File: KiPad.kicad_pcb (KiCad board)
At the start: 2 copper layers, 82 x 142.5 mm, 67 parts, among them J1 USB_C_Receptacle_USB2.0, SW1 SW_SPST_LED, SW10 SW_SPST, SW11 SW_SPST, SW12 SW_SPST, SW13 SW_SPST, SW14 SW_SPST, SW15 SW_SPST, SW16 SW_SPST, SW17 SW_SPST, SW18 SW_SPST, SW19 SW_SPST, SW2 SW_SPST_LED, SW20 SW_SPST, SW21 SW_SPST, SW3 SW_SPST_LED, SW4 SW_SPST_LED, SW5 SW_SPST, SW6 SW_SPST, SW7 SW_SPST, SW8 SW_SPST, SW9 SW_SPST, U1 ATmega32U4RC-A, Y1 16MHz

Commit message: v2
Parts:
- removed C1: 1u, Capacitor_SMD:C_0805_2012Metric
- removed C3, C4: 22p, Capacitor_SMD:C_0805_2012Metric
- removed the D21 at (155.0, 117.2)
- removed the D21 at (104.4, 116.9)
- removed F1: 500mA, Fuse:Fuse_1206_3216Metric
- removed R1, R2: 22, Resistor_SMD:R_0805_2012Metric
- removed R10, R11: 10k, Resistor_SMD:R_0805_2012Metric
- removed R3, R4: 5.1k, Resistor_SMD:R_0805_2012Metric
- removed SW_HWB1, SW_RST1: SW_Push, Button_Switch_SMD:SW_SPST_TL3342
- removed U1: ATmega32U4RC-A, Package_QFP:TQFP-44_10x10mm_P0.8mm
- removed Y1: 16MHz, Crystal:Crystal_SMD_3225-4Pin_3.2x2.5mm
- added D21: ~, Diode_SMD:D_MiniMELF, B.Cu at (100.3, 43.1)
- added J2: Conn_02x08_Counter_Clockwise, Connector_PinSocket_2.54mm:PinSocket_2x08_P2.54mm_Vertical, F.Cu at (149.5, 78.8)
- added kibuzzard-66936F3A: G***, kibuzzard-66936F3A, F.Cu at (36.0, 24.0)
- added kibuzzard-66936F5C: G***, kibuzzard-66936F5C, F.Cu at (45.5, 25.5)
- added kibuzzard-66936F83: G***, kibuzzard-66936F83, F.Cu at (93.8, 149.2)
- added kibuzzard-669374CF: G***, kibuzzard-669374CF, F.Cu at (143.5, 57.5)
- added kibuzzard-669374E3: G***, kibuzzard-669374E3, F.Cu at (144.8, 50.0)
- added kibuzzard-66937522: G***, kibuzzard-66937522, F.Cu at (145.8, 54.2)
- added kibuzzard-6693755C: G***, kibuzzard-6693755C, F.Cu at (154.0, 87.2)
- A1: footprint Custom:KB2040_SMD -> Custom:KB2040_THT
- C2, C5, R6, R7, R8, R9: moved to B.Cu
- J1: value USB_C_Receptacle_USB2.0 -> Conn_02x08_Counter_Clockwise; footprint Connector_USB:USB_C_Receptacle_GCT_USB4105-xx-A_16P_TopMnt_Horizontal -> Connector_PinSocket_2.54mm:PinSocket_2x08_P2.54mm_Vertical
- SW1, SW2, SW3, SW4: footprint Custom:MX-Solderable-1U-0805-LED -> Custom:MX-Hotswap-1U-0805-LED
- SW10, SW11, SW13, SW14, SW15, SW16, SW17, SW18, SW21, SW5, SW6, SW7, SW8, SW9: footprint MX_Solderable:MX-Solderable-1U -> MX_Hotswap:MX-Hotswap-1U
- SW12, SW19: footprint MX_Solderable:MX-Solderable-2U-Vertical -> MX_Hotswap:MX-Hotswap-2U-Vertical-ReversedStabilizers
- SW20: footprint MX_Solderable:MX-Solderable-2U -> MX_Hotswap:MX-Hotswap-2U
- moved R9 79.6 mm to (95.2, 43.5)
- moved R6 79.6 mm to (38.2, 43.5)
- moved R7 79.6 mm to (57.2, 43.5)
- moved R8 79.6 mm to (76.2, 43.5)
- moved D8 73.9 mm to (100.3, 95.5)
- moved SW12 73.9 mm to (95.2, 90.5)
- moved D1 73.9 mm to (43.2, 66.9)
- moved D12 73.9 mm to (43.2, 124.1)
- moved D13 73.9 mm to (62.2, 124.1)
- moved D14 73.9 mm to (81.3, 124.1)
- moved D15 73.9 mm to (100.3, 133.6)
- moved D16 73.9 mm to (52.7, 143.1)
- moved D17 73.9 mm to (81.3, 143.1)
- moved D18 73.9 mm to (43.2, 43.1)
- moved D19 73.9 mm to (62.2, 43.1)
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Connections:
- A1 pad 10: /R2 -> /MCU_C1
- A1 pad 11: /R3 -> /MCU_C2
- A1 pad 12: /R4 -> /MCU_C3
- A1 pad 13: /R5 -> /MCU_R0
- A1 pad 14: unconnected-(A1-D10-Pad14) -> /MCU_R1
- A1 pad 18: /LED_A -> /MCU_LED_A
- A1 pad 19: /LED_B -> /MCU_LED_B
- A1 pad 2: /C0 -> unconnected-(A1-D0-Pad2)
- A1 pad 20: /LED_C -> /MCU_LED_C
- A1 pad 21: /LED_D -> /MCU_LED_D
- A1 pad 22: +5V -> /MCU_VCC
- A1 pad 24: GND -> /MCU_GND
- A1 pad 3: /C1 -> /MCU_R2
- A1 pad 4: GND -> /MCU_GND
- A1 pad 5: GND -> /MCU_GND
- A1 pad 6: /C2 -> /MCU_R3
- A1 pad 7: /C3 -> /MCU_R4
- A1 pad 8: /R0 -> /MCU_R5
- A1 pad 9: /R1 -> /MCU_C0
- C2 pad 1: +5V -> +3V3
- C5 pad 1: +5V -> +3V3
- C6 pad 1: +5V -> +3V3
- C7 pad 1: +5V -> +3V3
- SW1 pad 4: +5V -> +3V3
- SW2 pad 4: +5V -> +3V3
- SW3 pad 4: +5V -> +3V3
- SW4 pad 4: +5V -> +3V3
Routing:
- net +5V: track 205.8 -> 0.00 mm, vias 7 -> 0
- net +3V3: track 0.00 -> 85.4 mm, vias 0 -> 4
- net /C0: track 149.4 -> 216.6 mm, vias 1 -> 6
- net /MCU_R2: track 0.00 -> 65.7 mm
- net /R2: track 164.3 -> 101.1 mm
- net /R1: track 131.2 -> 68.3 mm
- net /C1: track 109.7 -> 167.4 mm, vias 1 -> 5
- net /MCU_R3: track 0.00 -> 53.6 mm
- net /R4: track 202.3 -> 148.8 mm
- net /R3: track 165.4 -> 112.1 mm
- net /R5: track 194.0 -> 144.5 mm
- net GND: track 20.8 -> 68.7 mm, vias 5 -> 0
- net /MCU_R4: track 0.00 -> 46.5 mm
- net /MCU_C0: track 0.00 -> 39.8 mm
- net /MCU_R5: track 0.00 -> 39.2 mm
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- added copper zone on B.Cu, net /MCU_GND
- added copper zone on F.Cu, net /MCU_GND
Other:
- board size 82 x 142.5 mm -> 149.8 x 131.8 mm
- board text added: "JLCJLCJLCJLC"

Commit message: v3
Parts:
- removed A1: Adafruit Key Boar KB2040, Custom:KB2040_THT
- removed J2: Conn_02x08_Counter_Clockwise, Connector_PinSocket_2.54mm:PinSocket_2x08_P2.54mm_Vertical
- removed R6, R7, R8, R9: 470, Resistor_SMD:R_0805_2012Metric
- removed kibuzzard-66936F3A: G***, kibuzzard-66936F3A
- removed kibuzzard-66936F5C: G***, kibuzzard-66936F5C
- removed kibuzzard-66936F83: G***, kibuzzard-66936F83
- removed kibuzzard-669374CF: G***, kibuzzard-669374CF
- removed kibuzzard-669374E3: G***, kibuzzard-669374E3
- removed kibuzzard-66937522: G***, kibuzzard-66937522
- removed kibuzzard-6693755C: G***, kibuzzard-6693755C
- added C1: 22p, Capacitor_SMD:C_0402_1005Metric, B.Cu at (102.4, 120.5)
- added C3: 22p, Capacitor_SMD:C_0402_1005Metric, B.Cu at (102.2, 126.4)
- added LED1: SK6812MINI, Custom:LED_SK6812MINI-E_PLCC4_3.2x2.8mm_P1.75mm, B.Cu at (38.1, 32.6)
- added LED10: SK6812MINI, Custom:LED_SK6812MINI-E_PLCC4_3.2x2.8mm_P1.75mm, B.Cu at (57.1, 75.5)
- added LED11: SK6812MINI, Custom:LED_SK6812MINI-E_PLCC4_3.2x2.8mm_P1.75mm, B.Cu at (76.2, 75.5)
- added LED12: SK6812MINI, Custom:LED_SK6812MINI-E_PLCC4_3.2x2.8mm_P1.75mm, B.Cu at (95.2, 85.0)
- added LED13: SK6812MINI, Custom:LED_SK6812MINI-E_PLCC4_3.2x2.8mm_P1.75mm, B.Cu at (38.1, 94.5)
- added LED14: SK6812MINI, Custom:LED_SK6812MINI-E_PLCC4_3.2x2.8mm_P1.75mm, B.Cu at (57.1, 94.5)
- added LED15: SK6812MINI, Custom:LED_SK6812MINI-E_PLCC4_3.2x2.8mm_P1.75mm, B.Cu at (76.2, 94.5)
- added LED16: SK6812MINI, Custom:LED_SK6812MINI-E_PLCC4_3.2x2.8mm_P1.75mm, B.Cu at (38.1, 113.6)
- added LED17: SK6812MINI, Custom:LED_SK6812MINI-E_PLCC4_3.2x2.8mm_P1.75mm, B.Cu at (57.1, 113.6)
- added LED18: SK6812MINI, Custom:LED_SK6812MINI-E_PLCC4_3.2x2.8mm_P1.75mm, B.Cu at (76.2, 113.6)
- added LED19: SK6812MINI, Custom:LED_SK6812MINI-E_PLCC4_3.2x2.8mm_P1.75mm, B.Cu at (95.2, 123.1)
- added LED2: SK6812MINI, Custom:LED_SK6812MINI-E_PLCC4_3.2x2.8mm_P1.75mm, B.Cu at (57.1, 32.6)
- added LED20: SK6812MINI, Custom:LED_SK6812MINI-E_PLCC4_3.2x2.8mm_P1.75mm, B.Cu at (47.6, 132.6)
- added LED21: SK6812MINI, Custom:LED_SK6812MINI-E_PLCC4_3.2x2.8mm_P1.75mm, B.Cu at (76.2, 132.6)
- added LED3: SK6812MINI, Custom:LED_SK6812MINI-E_PLCC4_3.2x2.8mm_P1.75mm, B.Cu at (76.2, 32.6)
- added LED4: SK6812MINI, Custom:LED_SK6812MINI-E_PLCC4_3.2x2.8mm_P1.75mm, B.Cu at (95.2, 32.6)
- added LED5: SK6812MINI, Custom:LED_SK6812MINI-E_PLCC4_3.2x2.8mm_P1.75mm, B.Cu at (38.1, 56.4)
- added LED6: SK6812MINI, Custom:LED_SK6812MINI-E_PLCC4_3.2x2.8mm_P1.75mm, B.Cu at (57.1, 56.4)
- added LED7: SK6812MINI, Custom:LED_SK6812MINI-E_PLCC4_3.2x2.8mm_P1.75mm, B.Cu at (76.2, 56.4)
- added LED8: SK6812MINI, Custom:LED_SK6812MINI-E_PLCC4_3.2x2.8mm_P1.75mm, B.Cu at (95.2, 56.4)
- added LED9: SK6812MINI, Custom:LED_SK6812MINI-E_PLCC4_3.2x2.8mm_P1.75mm, B.Cu at (38.1, 75.5)
- added R1: 10k, Resistor_SMD:R_0402_1005Metric, B.Cu at (92.6, 105.3)
- added R2: 5.1k, Resistor_SMD:R_0402_1005Metric, F.Cu at (67.6, 28.6)
- added R3: 5.1k, Resistor_SMD:R_0402_1005Metric, F.Cu at (65.7, 28.6)
- added R4: 22, Resistor_SMD:R_0402_1005Metric, B.Cu at (66.0, 35.0)
- added R5: 22, Resistor_SMD:R_0402_1005Metric, B.Cu at (67.4, 35.0)
- added SW22: RESET, Resistor_SMD:R_0603_1608Metric, B.Cu at (91.2, 104.7)
- added U2: ATmega32U2-M, Package_DFN_QFN:QFN-32-1EP_5x5mm_P0.5mm_EP3.1x3.1mm, B.Cu at (96.4, 108.8)
- added Y1: 16MHz, Crystal:Crystal_SMD_3225-4Pin_3.2x2.5mm, B.Cu at (102.3, 123.5)
- added kibuzzard-669F6A5B: G***, kibuzzard-669F6A5B, F.Cu at (93.4, 27.4)
- added kibuzzard-669F6A5B: G***, kibuzzard-669F6A5B, B.Cu at (41.0, 27.4)
- added kibuzzard-669F6A61: G***, kibuzzard-669F6A61, F.Cu at (101.0, 28.3)
- added kibuzzard-669F6A61: G***, kibuzzard-669F6A61, B.Cu at (33.3, 28.3)
- added kibuzzard-669F6A7B: G***, kibuzzard-669F6A7B, F.Cu at (36.9, 148.8)
- added kibuzzard-669F6A7B: G***, kibuzzard-669F6A7B, B.Cu at (96.5, 148.8)
- C6: value 0.1u -> 1u; footprint Capacitor_SMD:C_0805_2012Metric -> Capacitor_SMD:C_0603_1608Metric
- J1: value Conn_02x08_Counter_Clockwise -> USB_C_Receptacle_USB2.0_14P; footprint Connector_PinSocket_2.54mm:PinSocket_2x08_P2.54mm_Vertical -> Connector_USB:USB_C_Receptacle_GCT_USB4105-xx-A_16P_TopMnt_Horizontal
- SW1: value SW_SPST_LED -> SW_A; footprint Custom:MX-Hotswap-1U-0805-LED -> MX_Hotswap:MX-Hotswap-1U
- SW10: value SW_SPST -> SW_8
- SW11: value SW_SPST -> SW_9
- SW12: value SW_SPST -> SW_ADD
- SW13: value SW_SPST -> SW_4
- SW14: value SW_SPST -> SW_5
- SW15: value SW_SPST -> SW_6
- SW16: value SW_SPST -> SW_1
- SW17: value SW_SPST -> SW_2
- SW18: value SW_SPST -> SW_3
- SW19: value SW_SPST -> SW_ENTER
- SW2: value SW_SPST_LED -> SW_B; footprint Custom:MX-Hotswap-1U-0805-LED -> MX_Hotswap:MX-Hotswap-1U
- SW20: value SW_SPST -> SW_0
- SW21: value SW_SPST -> SW_DOT
- SW3: value SW_SPST_LED -> SW_C; footprint Custom:MX-Hotswap-1U-0805-LED -> MX_Hotswap:MX-Hotswap-1U
- SW4: value SW_SPST_LED -> SW_D; footprint Custom:MX-Hotswap-1U-0805-LED -> MX_Hotswap:MX-Hotswap-1U
- SW5: value SW_SPST -> SW_NL
- SW6: value SW_SPST -> SW_DIV
- SW7: value SW_SPST -> SW_MUL
- SW8: value SW_SPST -> SW_SUB
- SW9: value SW_SPST -> SW_7
- moved D20 105.3 mm to (55.8, 145.3)
- moved D21 103.4 mm to (84.4, 145.3)
- moved D19 101.4 mm to (103.4, 135.8)
- moved D18 92.8 mm to (84.4, 126.3)
- moved D12 59.0 mm to (96.6, 99.1), turned to 0 degrees
- moved C6 57.4 mm to (94.8, 103.4), turned to 90 degrees
- moved C7 57.3 mm to (102.4, 105.7), turned to 0 degrees
- moved J1 43.5 mm to (66.7, 28.6), turned to 0 degrees
- moved C2 33.9 mm to (70.3, 35.7), turned to 0 degrees
- moved D15 30.8 mm to (84.4, 107.2)
- moved D8 26.6 mm to (103.4, 69.1)
- moved D17 23.2 mm to (65.3, 126.3)
- moved D14 23.2 mm to (65.3, 107.2)
- moved D13 23.2 mm to (46.3, 107.2)
- moved D1 21.9 mm to (46.3, 45.3)
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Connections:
- C2 pad 1: +3V3 -> +5V
- C5 pad 1: +3V3 -> +5V
- C6 pad 1: +3V3 -> Net-(U2-UCAP)
- C7 pad 1: +3V3 -> +5V
- D1 pad 1: /R1 -> /R0
- D10 pad 1: /R3 -> /R2
- D11 pad 1: /R3 -> /R2
- D12 pad 1: /R4 -> /R2
- D13 pad 1: /R4 -> /R3
- D14 pad 1: /R4 -> /R3
- D15 pad 1: /R4 -> /R3
- D16 pad 1: /R5 -> /R4
- D17 pad 1: /R5 -> /R4
- D18 pad 1: /R0 -> /R4
- D19 pad 1: /R0 -> /R4
- D2 pad 1: /R1 -> /R0
- D20 pad 1: /R0 -> /R5
- D21 pad 1: /R0 -> /R5
- D3 pad 1: /R1 -> /R0
- D4 pad 1: /R1 -> /R0
- D5 pad 1: /R2 -> /R1
- D6 pad 1: /R2 -> /R1
- D7 pad 1: /R2 -> /R1
- D8 pad 1: /R2 -> /R1
- D9 pad 1: /R3 -> /R2
- SW1 pad 1: Net-(D18-A) -> Net-(D1-A)
- SW10 pad 1: Net-(D6-A) -> Net-(D10-A)
- SW11 pad 1: Net-(D7-A) -> Net-(D11-A)
- SW12 pad 1: Net-(D8-A) -> Net-(D12-A)
- SW13 pad 1: Net-(D9-A) -> Net-(D13-A)
- SW14 pad 1: Net-(D10-A) -> Net-(D14-A)
- SW15 pad 1: Net-(D11-A) -> Net-(D15-A)
- SW16 pad 1: Net-(D12-A) -> Net-(D16-A)
- SW17 pad 1: Net-(D13-A) -> Net-(D17-A)
- SW18 pad 1: Net-(D14-A) -> Net-(D18-A)
- SW19 pad 1: Net-(D15-A) -> Net-(D19-A)
- SW2 pad 1: Net-(D19-A) -> Net-(D2-A)
- SW20 pad 1: Net-(D16-A) -> Net-(D20-A)
- SW21 pad 1: Net-(D17-A) -> Net-(D21-A)
- SW3 pad 1: Net-(D20-A) -> Net-(D3-A)
- SW4 pad 1: Net-(D21-A) -> Net-(D4-A)
- SW5 pad 1: Net-(D1-A) -> Net-(D5-A)
- SW6 pad 1: Net-(D2-A) -> Net-(D6-A)
- SW7 pad 1: Net-(D3-A) -> Net-(D7-A)
- SW8 pad 1: Net-(D4-A) -> Net-(D8-A)
- SW9 pad 1: Net-(D5-A) -> Net-(D9-A)
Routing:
- net +5V: track 0.00 -> 513.8 mm, vias 0 -> 9
- net /LED_DATA: track 0.00 -> 159.7 mm, vias 0 -> 4
- net /USB_DP: track 0.00 -> 103.3 mm, vias 0 -> 4
- net /USB_DN: track 0.00 -> 102.5 mm, vias 0 -> 2
- net +3V3: track 85.4 -> 0.00 mm, vias 4 -> 0
- net /LED_A: track 79.5 -> 0.00 mm, vias 2 -> 0
- net Net-(LED4-DOUT): track 0.00 -> 76.2 mm
- net Net-(LED8-DOUT): track 0.00 -> 75.4 mm
- net /R0: track 63.8 -> 135.9 mm, vias 0 -> 2
- net Net-(LED12-DOUT): track 0.00 -> 66.7 mm
- net /MCU_R2: track 65.7 -> 0.00 mm
- net /R3: track 112.1 -> 48.1 mm
- net Net-(LED19-DOUT): track 0.00 -> 62.5 mm
- net /LED_B: track 59.4 -> 0.00 mm, vias 2 -> 0
- net Net-(LED15-DOUT): track 0.00 -> 55.5 mm
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- removed copper zone on B.Cu, net /MCU_GND
- removed copper zone on F.Cu, net /MCU_GND
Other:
- board size 149.8 x 131.8 mm -> 81.9 x 126.7 mm
- board text removed: "JLCJLCJLCJLC"

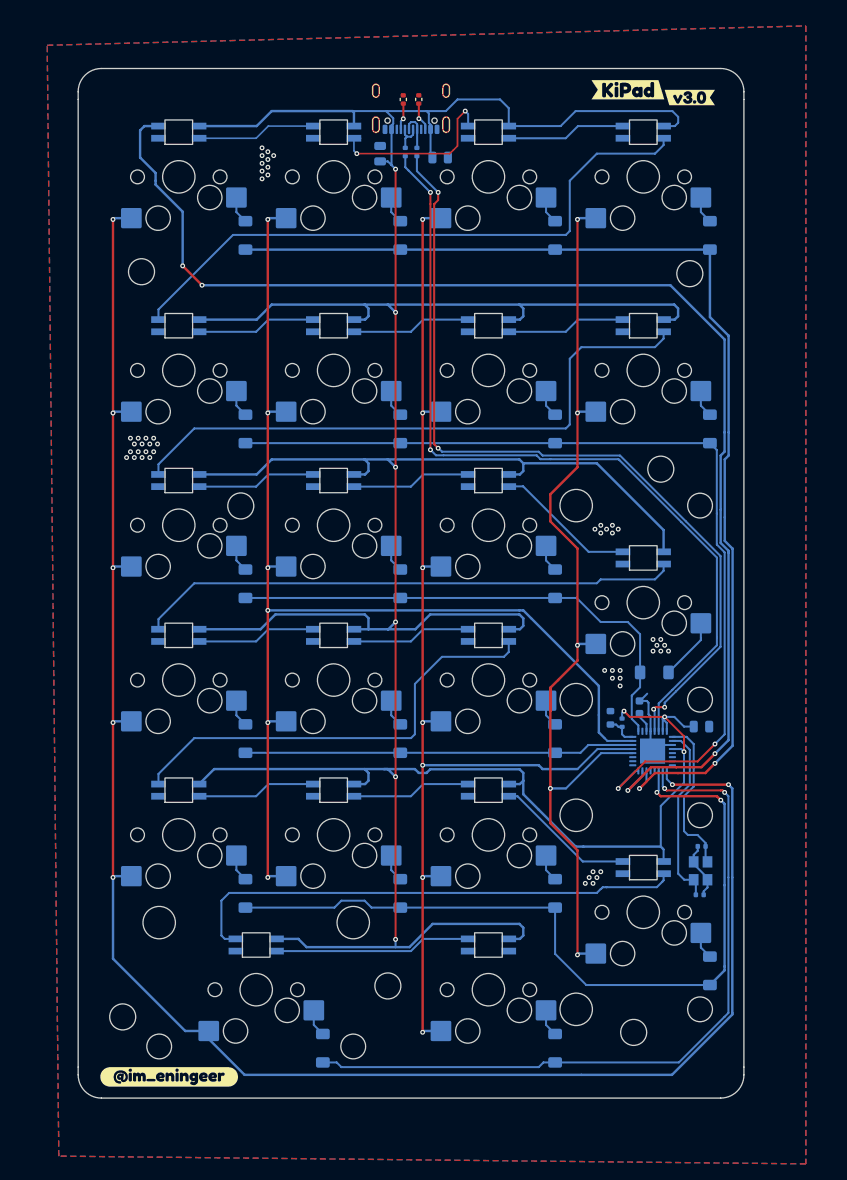
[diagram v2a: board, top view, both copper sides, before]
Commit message: v3.1
Flip around stabs so the shaft is on the outside.
Fix LED footprint and reroute.
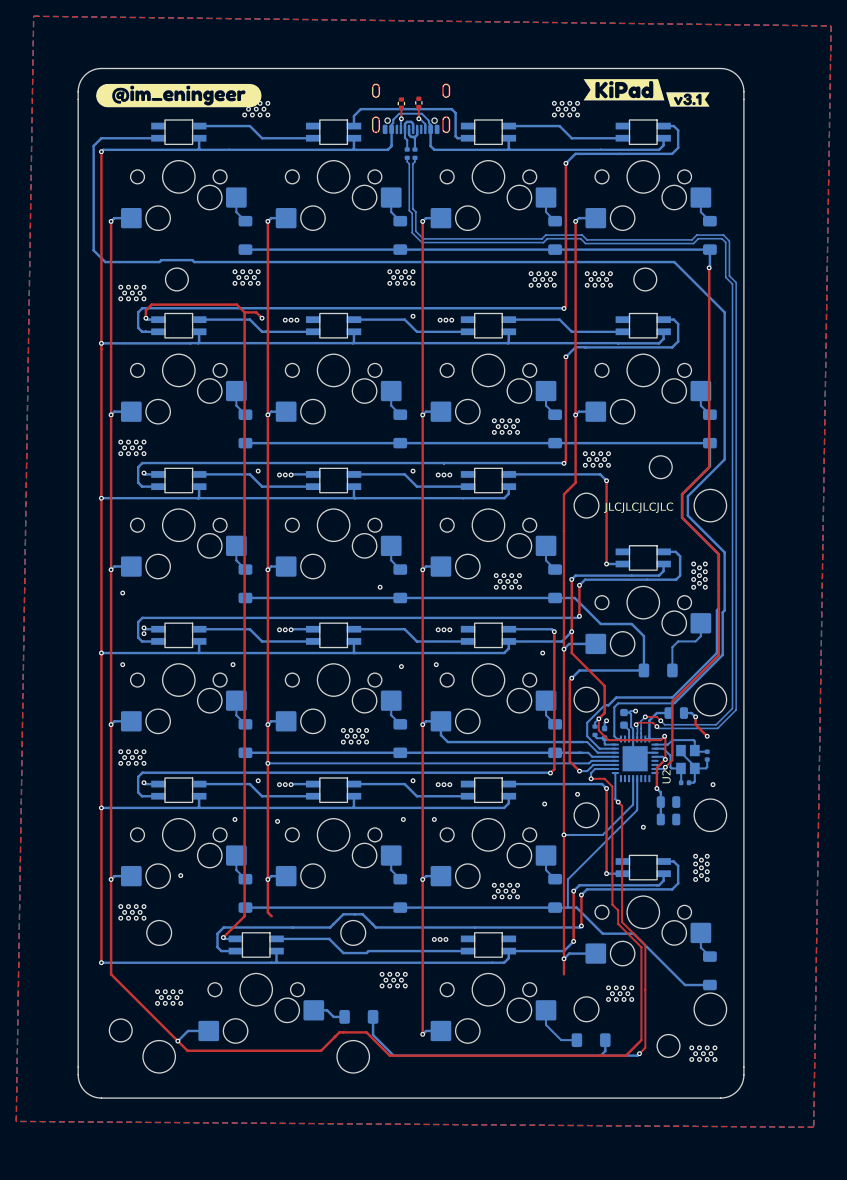
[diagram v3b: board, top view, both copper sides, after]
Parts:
- removed kibuzzard-669F6A5B (x2): G***, kibuzzard-669F6A5B
- removed kibuzzard-669F6A61 (x2): G***, kibuzzard-669F6A61
- removed kibuzzard-669F6A7B (x2): G***, kibuzzard-669F6A7B
- added kibuzzard-66A8A61F: G***, kibuzzard-66A8A61F, F.Cu at (100.7, 28.6)
- added kibuzzard-66A8A61F: G***, kibuzzard-66A8A61F, B.Cu at (31.4, 29.1)
- added kibuzzard-66A8A64C: G***, kibuzzard-66A8A64C, F.Cu at (92.9, 27.4)
- added kibuzzard-66A8A64C: G***, kibuzzard-66A8A64C, B.Cu at (39.3, 27.9)
- added kibuzzard-66A8A670: G***, kibuzzard-66A8A670, F.Cu at (38.1, 28.1)
- added kibuzzard-66A8A670: G***, kibuzzard-66A8A670, B.Cu at (95.0, 27.9)
- SW12, SW19: footprint MX_Hotswap:MX-Hotswap-2U-Vertical-ReversedStabilizers -> MX_Hotswap:MX-Hotswap-2U-Vertical
- SW20: footprint MX_Hotswap:MX-Hotswap-2U -> MX_Hotswap:MX-Hotswap-2U-ReversedStabilizers
- SW22: footprint Resistor_SMD:R_0603_1608Metric -> Resistor_SMD:R_0402_1005Metric_Pad0.72x0.64mm_HandSolder
- moved C2 84.1 mm to (98.4, 115.0)
- moved C5 77.9 mm to (99.3, 104.1), turned to 0 degrees
- moved C3 17.1 mm to (103.1, 109.3), turned to -90 degrees
- moved Y1 13.8 mm to (100.7, 109.8), turned to 90 degrees
- moved C7 12.1 mm to (98.4, 117.2)
- moved C1 8.10 mm to (100.4, 112.6), turned to 180 degrees
- moved D20 5.87 mm to (60.3, 141.5), turned to 180 degrees
- moved D21 4.54 mm to (88.8, 144.3), turned to 180 degrees
- moved R1 3.48 mm to (89.3, 106.2)
- moved C6 2.38 mm to (92.9, 104.8)
- moved U2 2.35 mm to (94.3, 109.7)
- moved SW22 2.04 mm to (90.5, 106.6)
- moved R3 0.56 mm to (65.5, 29.1)
- moved D12 0.53 mm to (97.1, 98.8)
- moved R2 0.43 mm to (67.6, 29.0)
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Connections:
- C1 pad 2: Net-(U2-XTAL1) -> Net-(U2-PC0/XTAL2)
- C3 pad 1: Net-(U2-PC0/XTAL2) -> Net-(U2-XTAL1)
- J1 pad A8: (no net) -> unconnected-(J1-SBU1-PadA8)
- J1 pad B8: (no net) -> unconnected-(J1-SBU2-PadB8)
- U2 pad 10: /R5 -> unconnected-(U2-PD4-Pad10)
- U2 pad 11: /R4 -> unconnected-(U2-PD5-Pad11)
- U2 pad 12: unconnected-(U2-PD6-Pad12) -> /R4
- U2 pad 13: unconnected-(U2-~{HWB}/PD7-Pad13) -> /C3
- U2 pad 14: /R0 -> unconnected-(U2-PB0-Pad14)
- U2 pad 15: /LED_DATA -> unconnected-(U2-PB1-Pad15)
- U2 pad 16: /R1 -> unconnected-(U2-PB2-Pad16)
- U2 pad 17: unconnected-(U2-PB3-Pad17) -> /R5
- U2 pad 18: unconnected-(U2-PB4-Pad18) -> /C0
- U2 pad 19: unconnected-(U2-PB5-Pad19) -> /R2
- U2 pad 20: /C3 -> /C1
- U2 pad 21: /C2 -> /R3
- U2 pad 22: /R3 -> /C2
- U2 pad 23: /C1 -> /R1
- U2 pad 25: /R2 -> /LED_DATA
- U2 pad 7: unconnected-(U2-PD1-Pad7) -> /R0
- U2 pad 9: /C0 -> unconnected-(U2-PD3-Pad9)
- Y1 pad 1: Net-(U2-XTAL1) -> Net-(U2-PC0/XTAL2)
- Y1 pad 3: Net-(U2-PC0/XTAL2) -> Net-(U2-XTAL1)
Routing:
- net GND: track 18.5 -> 135.0 mm, vias 52 -> 290
- net +5V: track 513.8 -> 569.9 mm, vias 9 -> 14
- net Net-(LED15-DOUT): track 55.5 -> 78.9 mm, vias 0 -> 2
- net /USB_DN: track 102.5 -> 122.0 mm
- net /USB_DP: track 103.3 -> 122.8 mm, vias 4 -> 2
- net /R4: track 99.8 -> 80.5 mm, vias 2 -> 0
- net /R2: track 63.1 -> 81.2 mm, vias 0 -> 2
- net Net-(LED4-DOUT): track 76.2 -> 93.9 mm, vias 0 -> 2
- net Net-(U2-PC0/XTAL2): track 22.6 -> 6.81 mm
- net /R5: track 90.1 -> 74.6 mm
- net Net-(LED8-DOUT): track 75.4 -> 89.2 mm, vias 0 -> 2
- net Net-(LED12-DOUT): track 66.7 -> 80.5 mm, vias 0 -> 2
- net Net-(U2-XTAL1): track 19.9 -> 8.15 mm
- net /LED_DATA: track 159.7 -> 168.7 mm, vias 4 -> 0
- net Net-(LED19-DOUT): track 62.5 -> 71.1 mm, vias 0 -> 2
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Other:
- outline, holes or cut-outs redrawn
- board text added: "JLCJLCJLCJLC"
